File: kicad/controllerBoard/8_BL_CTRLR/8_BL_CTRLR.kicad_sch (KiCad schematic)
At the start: 16 parts, among them Q369 NMOS, Q370 NMOS, Q371 NMOS, Q372 NMOS, Q373 NMOS, Q374 NMOS, Q375 NMOS, Q376 NMOS

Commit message: did stuff
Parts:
- renumbered Q369 to Q370, Q370 to Q371, Q371 to Q372, Q372 to Q373, Q373 to Q374, Q374 to Q375, Q375 to Q376, Q376 to Q377, R4 to R10, R5 to R11, R6 to R12, R7 to R13, R8 to R14, R1 to R7, R2 to R8, R3 to R9

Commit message: did more simulation, added bom
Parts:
- renumbered Q370 to Q369, Q371 to Q370, Q372 to Q371, Q373 to Q372, Q374 to Q373, Q375 to Q374, Q376 to Q375, Q377 to Q376, R7 to R1, R8 to R2, R9 to R3, R10 to R4, R11 to R5, R12 to R6, R13 to R7, R14 to R8

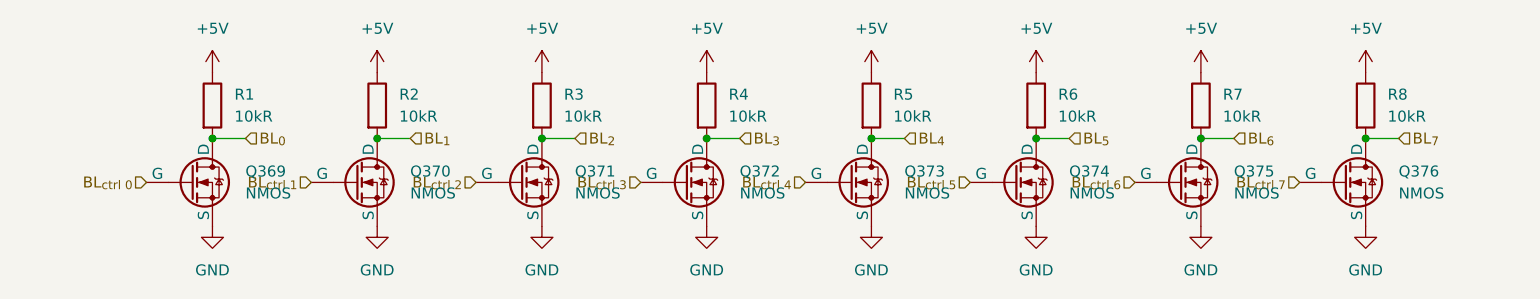
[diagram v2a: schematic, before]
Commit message: update main board schematic
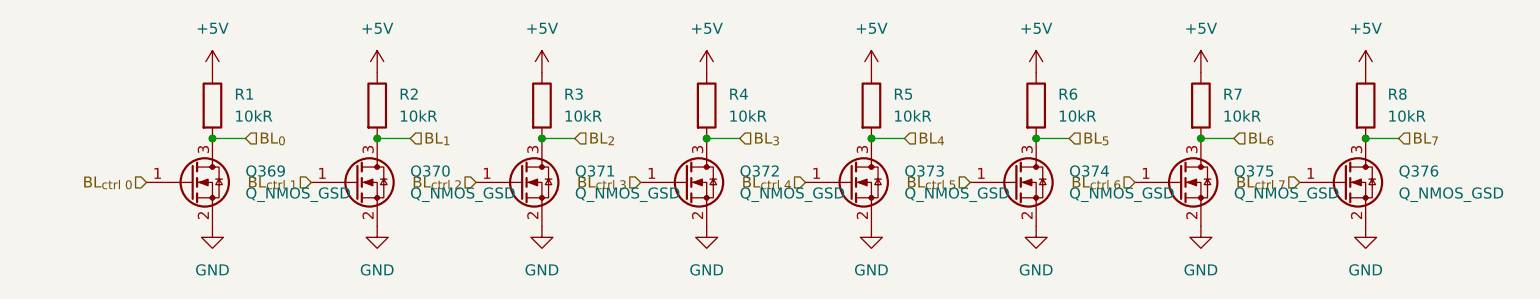
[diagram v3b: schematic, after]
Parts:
- Q369, Q370, Q371, Q372, Q373, Q374, Q375, Q376: value NMOS -> Q_NMOS_GSD; footprint (none) -> easyeda2kicad:SOT-23-N; symbol Simulation_SPICE:NMOS -> Transistor_FET:Q_NMOS_GSD
- R1, R2, R3, R4, R5, R6, R7, R8: footprint (none) -> Resistor_SMD:R_0805_2012Metric
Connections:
- net BL_{0}: now also Q369.3 (D); no longer Q369.1 (D)
- net BL_{1}: now also Q370.3 (D); no longer Q370.1 (D)
- net BL_{2}: now also Q371.3 (D); no longer Q371.1 (D)
- net BL_{3}: now also Q372.3 (D); no longer Q372.1 (D)
- net BL_{4}: now also Q373.3 (D); no longer Q373.1 (D)
- net BL_{5}: now also Q374.3 (D); no longer Q374.1 (D)
- net BL_{6}: now also Q375.3 (D); no longer Q375.1 (D)
- net BL_{7}: now also Q376.3 (D); no longer Q376.1 (D)
- net BL_{ctrl 0}: now also Q369.1 (G); no longer Q369.2 (G)
- net BL_{ctrl 1}: now also Q370.1 (G); no longer Q370.2 (G)
- net BL_{ctrl 2}: now also Q371.1 (G); no longer Q371.2 (G)
- net BL_{ctrl 3}: now also Q372.1 (G); no longer Q372.2 (G)
- net BL_{ctrl 4}: now also Q373.1 (G); no longer Q373.2 (G)
- net BL_{ctrl 5}: now also Q374.1 (G); no longer Q374.2 (G)
- net BL_{ctrl 6}: now also Q375.1 (G); no longer Q375.2 (G)
- net BL_{ctrl 7}: now also Q376.1 (G); no longer Q376.2 (G)
- net GND: now also Q369.2 (S), Q370.2 (S), Q371.2 (S), Q372.2 (S), Q373.2 (S), Q374.2 (S), Q375.2 (S), Q376.2 (S); no longer Q369.3 (S), Q370.3 (S), Q371.3 (S), Q372.3 (S), Q373.3 (S), Q374.3 (S), Q375.3 (S), Q376.3 (S)

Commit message: continue routing main controller board
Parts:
- renumbered Q369 to Q1, Q370 to Q2, Q371 to Q3, Q372 to Q4, Q373 to Q5, Q374 to Q6, Q375 to Q7, Q376 to Q8
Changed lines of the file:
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@@
 		(dnp no)
 		(fields_autoplaced yes)
-		(property "Reference" "Q372"
+		(property "Reference" "Q4"
 			(at 130.81 67.3099 0)
 			(show_name no)
@@
 			(project "8_BL_CTRLR"
 				(path "/97437f80-2620-4be2-b56e-738318932f5c"
-					(reference "Q372")
+					(reference "Q4")
 					(unit 1)
 				)
@@
 		(dnp no)
 		(fields_autoplaced yes)
-		(property "Reference" "#PWR070"
+		(property "Reference" "#PWR016"
 			(at 203.2 80.01 0)
 			(hide yes)
@@
 			(project "8_BL_CTRLR"
 				(path "/97437f80-2620-4be2-b56e-738318932f5c"
-					(reference "#PWR070")
+					(reference "#PWR016")
 					(unit 1)
 				)
@@
 		(dnp no)
 		(fields_autoplaced yes)
-		(property "Reference" "Q370"
+		(property "Reference" "Q2"
 			(at 92.71 67.3099 0)
 			(show_name no)
@@
 			(project "8_BL_CTRLR"
 				(path "/97437f80-2620-4be2-b56e-738318932f5c"
-					(reference "Q370")
+					(reference "Q2")
 					(unit 1)
 				)
@@
 		(dnp no)
 		(fields_autoplaced yes)
-		(property "Reference" "#PWR065"
+		(property "Reference" "#PWR011"
 			(at 165.1 59.69 0)
 			(hide yes)
@@
 			(project "8_BL_CTRLR"
 				(path "/97437f80-2620-4be2-b56e-738318932f5c"
-					(reference "#PWR065")
+					(reference "#PWR011")
 					(unit 1)
 				)
@@
 		(dnp no)
 		(fields_autoplaced yes)
-		(property "Reference" "Q371"
+		(property "Reference" "Q3"
 			(at 111.76 67.3099 0)
 			(show_name no)
@@
 			(project "8_BL_CTRLR"
 				(path "/97437f80-2620-4be2-b56e-738318932f5c"
-					(reference "Q371")
+					(reference "Q3")
 					(unit 1)
 				)
@@
 		(dnp no)
 		(fields_autoplaced yes)
-		(property "Reference" "Q375"
+		(property "Reference" "Q7"
 			(at 187.96 67.3099 0)
 			(show_name no)
@@
 			(project "8_BL_CTRLR"
 				(path "/97437f80-2620-4be2-b56e-738318932f5c"
-					(reference "Q375")
+					(reference "Q7")
 					(unit 1)
 				)
@@
 		(dnp no)
 		(fields_autoplaced yes)
-		(property "Reference" "Q374"
+		(property "Reference" "Q6"
 			(at 168.91 67.3099 0)
 			(show_name no)
@@
 			(project "8_BL_CTRLR"
 				(path "/97437f80-2620-4be2-b56e-738318932f5c"
-					(reference "Q374")
+					(reference "Q6")
 					(unit 1)
 				)
@@
 		(dnp no)
 		(fields_autoplaced yes)
-		(property "Reference" "#PWR067"
+		(property "Reference" "#PWR013"
 			(at 184.15 59.69 0)
 			(hide yes)
@@
 			(project "8_BL_CTRLR"
 				(path "/97437f80-2620-4be2-b56e-738318932f5c"
-					(reference "#PWR067")
+					(reference "#PWR013")
 					(unit 1)
 				)
@@
 		(dnp no)
 		(fields_autoplaced yes)
-		(property "Reference" "#PWR064"
+		(property "Reference" "#PWR010"
 			(at 146.05 80.01 0)
 			(hide yes)
@@
 			(project "8_BL_CTRLR"
 				(path "/97437f80-2620-4be2-b56e-738318932f5c"
-					(reference "#PWR064")
+					(reference "#PWR010")
 					(unit 1)
 				)
@@
 		(dnp no)
 		(fields_autoplaced yes)
-		(property "Reference" "#PWR058"
+		(property "Reference" "#PWR04"
 			(at 88.9 80.01 0)
 			(hide yes)
@@
 			(project "8_BL_CTRLR"
 				(path "/97437f80-2620-4be2-b56e-738318932f5c"
-					(reference "#PWR058")
+					(reference "#PWR04")
 					(unit 1)
 				)
@@
 		(dnp no)
 		(fields_autoplaced yes)
-		(property "Reference" "#PWR057"
+		(property "Reference" "#PWR03"
 			(at 88.9 59.69 0)
 			(hide yes)
@@
 			(project "8_BL_CTRLR"
 				(path "/97437f80-2620-4be2-b56e-738318932f5c"
-					(reference "#PWR057")
+					(reference "#PWR03")
 					(unit 1)
 				)
@@
 		(dnp no)
 		(fields_autoplaced yes)
-		(property "Reference" "#PWR066"
+		(property "Reference" "#PWR012"
 			(at 165.1 80.01 0)
 			(hide yes)
@@
 			(project "8_BL_CTRLR"
 				(path "/97437f80-2620-4be2-b56e-738318932f5c"
-					(reference "#PWR066")
+					(reference "#PWR012")
 					(unit 1)
 				)
@@
 		(dnp no)
 		(fields_autoplaced yes)
-		(property "Reference" "Q376"
+		(property "Reference" "Q8"
 			(at 207.01 67.3099 0)
 			(show_name no)
@@
 			(project "8_BL_CTRLR"
 				(path "/97437f80-2620-4be2-b56e-738318932f5c"
-					(reference "Q376")
+					(reference "Q8")
 					(unit 1)
 				)
@@
 		(dnp no)
 		(fields_autoplaced yes)
-		(property "Reference" "#PWR056"
+		(property "Reference" "#PWR02"
 			(at 69.85 80.01 0)
 			(hide yes)
@@
 			(project "8_BL_CTRLR"
 				(path "/97437f80-2620-4be2-b56e-738318932f5c"
-					(reference "#PWR056")
+					(reference "#PWR02")
 					(unit 1)
 				)
@@
 		(dnp no)
 		(fields_autoplaced yes)
-		(property "Reference" "#PWR062"
+		(property "Reference" "#PWR08"
 			(at 127 80.01 0)
 			(hide yes)
@@
 			(project "8_BL_CTRLR"
 				(path "/97437f80-2620-4be2-b56e-738318932f5c"
-					(reference "#PWR062")
+					(reference "#PWR08")
 					(unit 1)
 				)
@@
 		(dnp no)
 		(fields_autoplaced yes)
-		(property "Reference" "Q373"
+		(property "Reference" "Q5"
 			(at 149.86 67.3099 0)
 			(show_name no)
@@
 			(project "8_BL_CTRLR"
 				(path "/97437f80-2620-4be2-b56e-738318932f5c"
-					(reference "Q373")
+					(reference "Q5")
 					(unit 1)
 				)
@@
 		(dnp no)
 		(fields_autoplaced yes)
-		(property "Reference" "#PWR063"
+		(property "Reference" "#PWR09"
 			(at 146.05 59.69 0)
 			(hide yes)
@@
 			(project "8_BL_CTRLR"
 				(path "/97437f80-2620-4be2-b56e-738318932f5c"
-					(reference "#PWR063")
+					(reference "#PWR09")
 					(unit 1)
 				)
@@
 		(dnp no)
 		(fields_autoplaced yes)
-		(property "Reference" "#PWR055"
+		(property "Reference" "#PWR01"
 			(at 69.85 59.69 0)
 			(hide yes)
@@
 			(project "8_BL_CTRLR"
 				(path "/97437f80-2620-4be2-b56e-738318932f5c"
-					(reference "#PWR055")
+					(reference "#PWR01")
 					(unit 1)
 				)
@@
 		(dnp no)
 		(fields_autoplaced yes)
-		(property "Reference" "#PWR061"
+		(property "Reference" "#PWR07"
 			(at 127 59.69 0)
 			(hide yes)
@@
 			(project "8_BL_CTRLR"
 				(path "/97437f80-2620-4be2-b56e-738318932f5c"
-					(reference "#PWR061")
+					(reference "#PWR07")
 					(unit 1)
 				)
@@
 		(dnp no)
 		(fields_autoplaced yes)
-		(property "Reference" "#PWR060"
+		(property "Reference" "#PWR06"
 			(at 107.95 80.01 0)
 			(hide yes)
@@
 			(project "8_BL_CTRLR"
 				(path "/97437f80-2620-4be2-b56e-738318932f5c"
-					(reference "#PWR060")
+					(reference "#PWR06")
 					(unit 1)
 				)
@@
 		(dnp no)
 		(fields_autoplaced yes)
-		(property "Reference" "#PWR069"
+		(property "Reference" "#PWR015"
 			(at 203.2 59.69 0)
 			(hide yes)
@@
 			(project "8_BL_CTRLR"
 				(path "/97437f80-2620-4be2-b56e-738318932f5c"
-					(reference "#PWR069")
+					(reference "#PWR015")
 					(unit 1)
 				)
@@
 		(dnp no)
 		(fields_autoplaced yes)
-		(property "Reference" "#PWR059"
+		(property "Reference" "#PWR05"
 			(at 107.95 59.69 0)
 			(hide yes)
@@
 			(project "8_BL_CTRLR"
 				(path "/97437f80-2620-4be2-b56e-738318932f5c"
-					(reference "#PWR059")
+					(reference "#PWR05")
 					(unit 1)
 				)
@@
 		(dnp no)
 		(fields_autoplaced yes)
-		(property "Reference" "Q369"
+		(property "Reference" "Q1"
 			(at 73.66 67.3099 0)
 			(show_name no)
@@
 			(project "8_BL_CTRLR"
 				(path "/97437f80-2620-4be2-b56e-738318932f5c"
-					(reference "Q369")
+					(reference "Q1")
 					(unit 1)
 				)
@@
 		(dnp no)
 		(fields_autoplaced yes)
-		(property "Reference" "#PWR068"
+		(property "Reference" "#PWR014"
 			(at 184.15 80.01 0)
 			(hide yes)
@@
 			(project "8_BL_CTRLR"
 				(path "/97437f80-2620-4be2-b56e-738318932f5c"
-					(reference "#PWR068")
+					(reference "#PWR014")
 					(unit 1)
 				)
@@
 		)
 	)
+	(embedded_fonts no)
 )

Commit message: finished routing all sub schematics
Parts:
- renumbered Q1 to Q369, Q2 to Q370, Q3 to Q371, Q4 to Q372, Q5 to Q373, Q6 to Q374, Q7 to Q375, Q8 to Q376
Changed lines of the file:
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@@
 		(dnp no)
 		(fields_autoplaced yes)
-		(property "Reference" "Q4"
+		(property "Reference" "Q372"
 			(at 130.81 67.3099 0)
 			(show_name no)
@@
 		(dnp no)
 		(fields_autoplaced yes)
-		(property "Reference" "#PWR016"
+		(property "Reference" "#PWR070"
 			(at 203.2 80.01 0)
 			(hide yes)
@@
 		(dnp no)
 		(fields_autoplaced yes)
-		(property "Reference" "Q2"
+		(property "Reference" "Q370"
 			(at 92.71 67.3099 0)
 			(show_name no)
@@
 		(dnp no)
 		(fields_autoplaced yes)
-		(property "Reference" "#PWR011"
+		(property "Reference" "#PWR065"
 			(at 165.1 59.69 0)
 			(hide yes)
@@
 		(dnp no)
 		(fields_autoplaced yes)
-		(property "Reference" "Q3"
+		(property "Reference" "Q371"
 			(at 111.76 67.3099 0)
 			(show_name no)
@@
 		(dnp no)
 		(fields_autoplaced yes)
-		(property "Reference" "Q7"
+		(property "Reference" "Q375"
 			(at 187.96 67.3099 0)
 			(show_name no)
@@
 		(dnp no)
 		(fields_autoplaced yes)
-		(property "Reference" "Q6"
+		(property "Reference" "Q374"
 			(at 168.91 67.3099 0)
 			(show_name no)
@@
 		(dnp no)
 		(fields_autoplaced yes)
-		(property "Reference" "#PWR013"
+		(property "Reference" "#PWR067"
 			(at 184.15 59.69 0)
 			(hide yes)
@@
 		(dnp no)
 		(fields_autoplaced yes)
-		(property "Reference" "#PWR010"
+		(property "Reference" "#PWR064"
 			(at 146.05 80.01 0)
 			(hide yes)
@@
 		(dnp no)
 		(fields_autoplaced yes)
-		(property "Reference" "#PWR04"
+		(property "Reference" "#PWR058"
 			(at 88.9 80.01 0)
 			(hide yes)
@@
 		(dnp no)
 		(fields_autoplaced yes)
-		(property "Reference" "#PWR03"
+		(property "Reference" "#PWR057"
 			(at 88.9 59.69 0)
 			(hide yes)
@@
 		(dnp no)
 		(fields_autoplaced yes)
-		(property "Reference" "#PWR012"
+		(property "Reference" "#PWR066"
 			(at 165.1 80.01 0)
 			(hide yes)
@@
 		(dnp no)
 		(fields_autoplaced yes)
-		(property "Reference" "Q8"
+		(property "Reference" "Q376"
 			(at 207.01 67.3099 0)
 			(show_name no)
@@
 		(dnp no)
 		(fields_autoplaced yes)
-		(property "Reference" "#PWR02"
+		(property "Reference" "#PWR056"
 			(at 69.85 80.01 0)
 			(hide yes)
@@
 		(dnp no)
 		(fields_autoplaced yes)
-		(property "Reference" "#PWR08"
+		(property "Reference" "#PWR062"
 			(at 127 80.01 0)
 			(hide yes)
@@
 		(dnp no)
 		(fields_autoplaced yes)
-		(property "Reference" "Q5"
+		(property "Reference" "Q373"
 			(at 149.86 67.3099 0)
 			(show_name no)
@@
 		(dnp no)
 		(fields_autoplaced yes)
-		(property "Reference" "#PWR09"
+		(property "Reference" "#PWR063"
 			(at 146.05 59.69 0)
 			(hide yes)
@@
 		(dnp no)
 		(fields_autoplaced yes)
-		(property "Reference" "#PWR01"
+		(property "Reference" "#PWR055"
 			(at 69.85 59.69 0)
 			(hide yes)
@@
 		(dnp no)
 		(fields_autoplaced yes)
-		(property "Reference" "#PWR07"
+		(property "Reference" "#PWR061"
 			(at 127 59.69 0)
 			(hide yes)
@@
 		(dnp no)
 		(fields_autoplaced yes)
-		(property "Reference" "#PWR06"
+		(property "Reference" "#PWR060"
 			(at 107.95 80.01 0)
 			(hide yes)
@@
 		(dnp no)
 		(fields_autoplaced yes)
-		(property "Reference" "#PWR015"
+		(property "Reference" "#PWR069"
 			(at 203.2 59.69 0)
 			(hide yes)
@@
 		(dnp no)
 		(fields_autoplaced yes)
-		(property "Reference" "#PWR05"
+		(property "Reference" "#PWR059"
 			(at 107.95 59.69 0)
 			(hide yes)
@@
 		(dnp no)
 		(fields_autoplaced yes)
-		(property "Reference" "Q1"
+		(property "Reference" "Q369"
 			(at 73.66 67.3099 0)
 			(show_name no)
@@
 		(dnp no)
 		(fields_autoplaced yes)
-		(property "Reference" "#PWR014"
+		(property "Reference" "#PWR068"
 			(at 184.15 80.01 0)
 			(hide yes)
@@
 		)
 	)
-	(embedded_fonts no)
 )

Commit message: update bom, add more capacitors
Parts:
- renumbered R6 to R10, R7 to R11, R8 to R12, R1 to R5, R2 to R6, R3 to R7, R4 to R8, R5 to R9
